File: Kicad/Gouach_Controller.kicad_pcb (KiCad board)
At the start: 4 copper layers, 41 x 104 mm, 139 parts, among them J1 HALL/Encoder, J10 USB, J11 CAN, J12 Serial, J2 Peripherals, J3 Peripherals, J4 IN+, J5 IN-, J6 MOTOR3, J7 MOTOR2, J8 MOTOR1, J9 SWD, Q1 IRFB7530, Q2 IRFB7530, Q3 IRFB7530, Q4 IRFB7530, Q5 IRFB7530, Q6 IRFB7530, Q7 DMN3300U, U1 STM32F405RGT6, U2 XC6220B331MR, U3 DRV8302, U4 SN65HVD232, U5 TPS54360DDA, U6 USBLC6-2SC6, Y2 8MHz

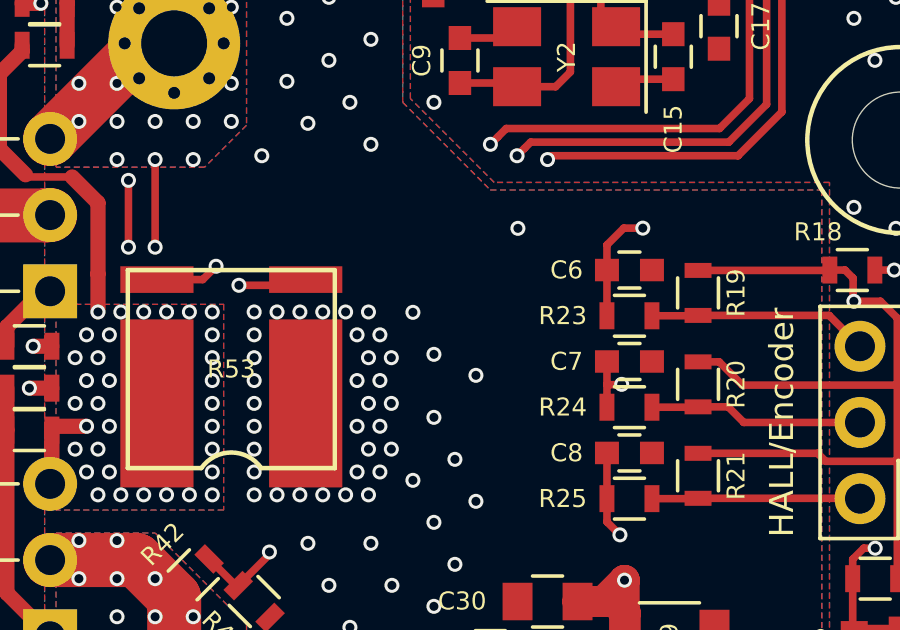
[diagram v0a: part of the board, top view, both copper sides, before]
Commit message: gouach logo
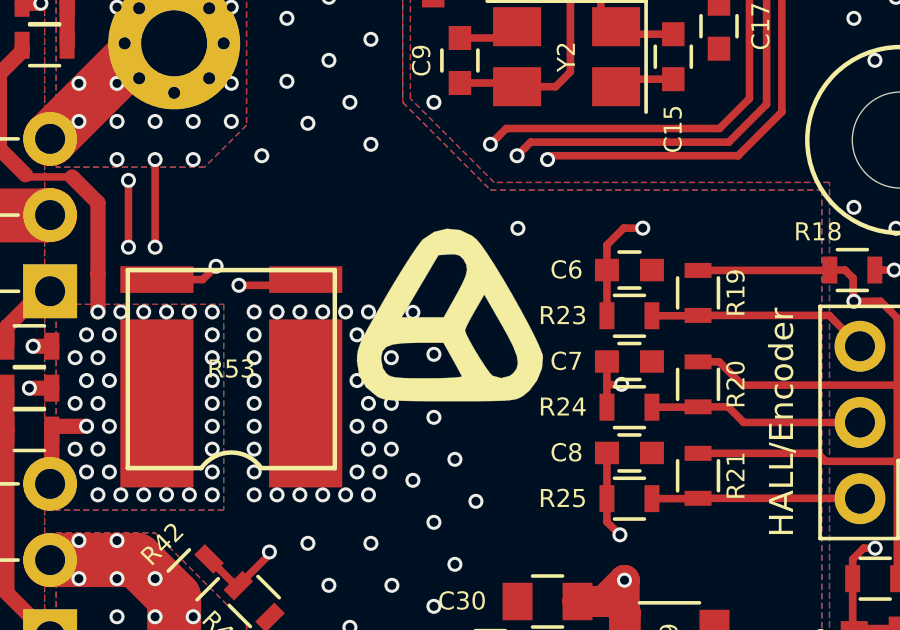
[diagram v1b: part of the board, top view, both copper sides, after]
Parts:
- removed the G*** at (120.4, 137.3)
- added G***: LOGO, logos:logotype, B.Cu at (119.5, 103.7)
- added G***: LOGO, logos:picto, F.Cu at (120.0, 85.6)
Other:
- board text added: "V1.0"

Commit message: changed all componenents to know version
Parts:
- removed G***: LOGO, logos:logotype
- removed G***: LOGO, logos:picto
- added U7: picto, logos:picto, F.Cu at (120.5, 87.1)
- added U8: logo, logos:logotype, B.Cu at (120.4, 97.4)
- C1, C10, C11, C12, C13, C14, C15, C16, C17, C18, C19, C2, C20, C21, C22, C23, C24, C25, C26, C27, C28, C32, C33, C34, C35, C36, C37, C39, C4, C46, C47, C5, C51, C52, C53, C56, C6, C7, C8, C9: footprint Capacitors_SMD:C_0603 -> Capacitor_SMD:C_0603_1608Metric
- C29, C3, C31, C49, C50, C55: footprint Capacitors_SMD:C_1210 -> Capacitor_SMD:C_1210_3225Metric
- C30, C38: footprint Capacitors_SMD:C_0805 -> Capacitor_SMD:C_0805_2012Metric
- C40, C41, C43, C44: footprint Capacitors_SMD:C_1206 -> Capacitor_SMD:C_1206_3216Metric
- C48: value 15uF/100V -> 15uF
- R1, R10, R11, R12, R13, R14, R15, R16, R17, R18, R19, R2, R20, R21, R22, R23, R24, R25, R26, R27, R28, R29, R3, R30, R31, R32, R33, R34, R35, R36, R37, R38, R39, R4, R40, R41, R42, R43, R44, R45, R46, R47, R5, R6, R7, R8, R9: footprint Resistors_SMD:R_0603 -> Resistor_SMD:R_0603_1608Metric
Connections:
- U1 pad 2: Net-(U1-Pad2) -> (no net)
- U1 pad 20: Net-(U1-Pad20) -> (no net)
- U1 pad 23: Net-(U1-Pad23) -> (no net)
- U1 pad 28: Net-(U1-Pad28) -> (no net)
- U1 pad 3: Net-(U1-Pad3) -> (no net)
- U1 pad 37: Net-(U1-Pad37) -> (no net)
- U1 pad 38: Net-(U1-Pad38) -> (no net)
- U1 pad 4: Net-(U1-Pad4) -> (no net)
- U1 pad 50: Net-(U1-Pad50) -> (no net)
- U1 pad 54: Net-(U1-Pad54) -> (no net)
- U1 pad 55: Net-(U1-Pad55) -> (no net)
- U1 pad 56: Net-(U1-Pad56) -> (no net)
- U2 pad 4: Net-(U2-Pad4) -> (no net)
- U3 pad 4: Net-(U3-Pad4) -> (no net)
- U3 pad 5: Net-(U3-Pad5) -> (no net)
- U3 pad 55: Net-(U3-Pad55) -> (no net)
- U3 pad 56: Net-(U3-Pad56) -> (no net)
- U4 pad 5: Net-(U4-Pad5) -> (no net)
- U4 pad 8: Net-(U4-Pad8) -> (no net)
- U5 pad 3: Net-(U5-Pad3) -> (no net)

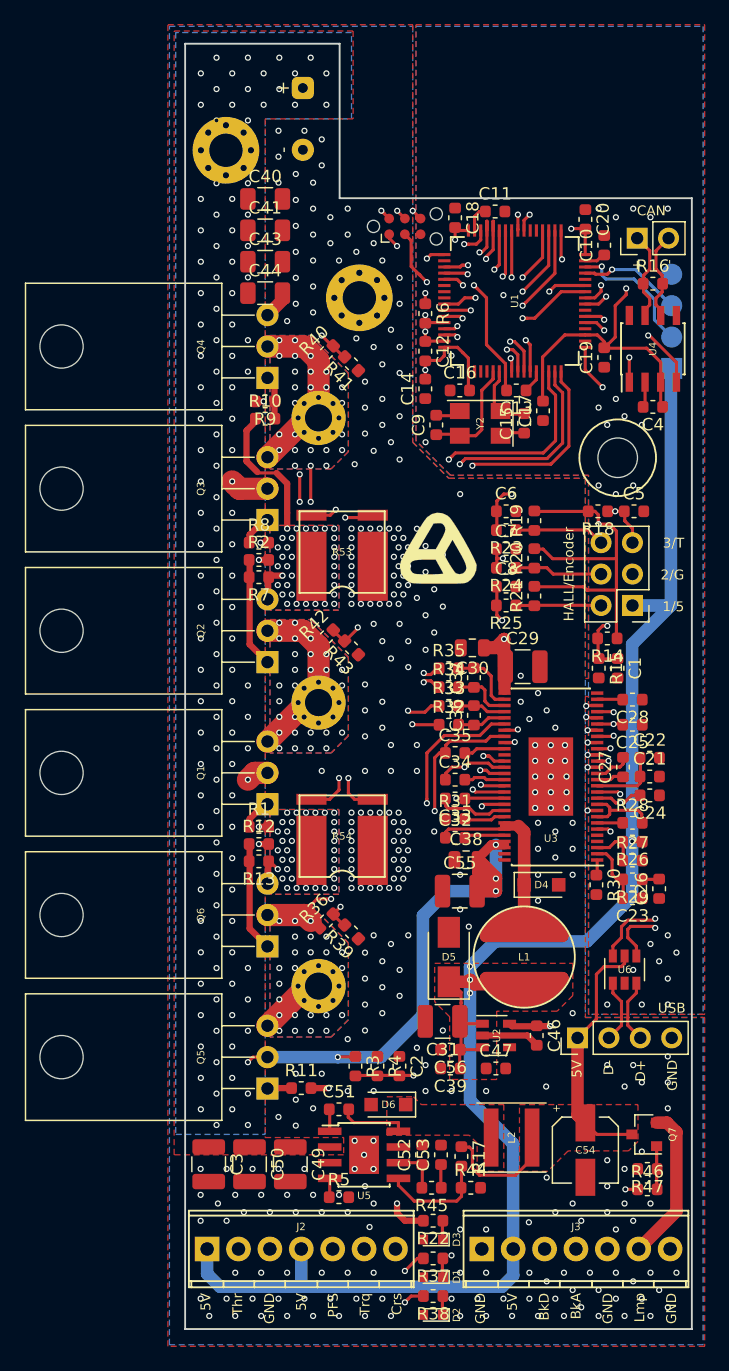
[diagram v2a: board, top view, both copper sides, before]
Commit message: Modified silkscreens. Changed peripheral connectors. Fixed some 3D libs paths
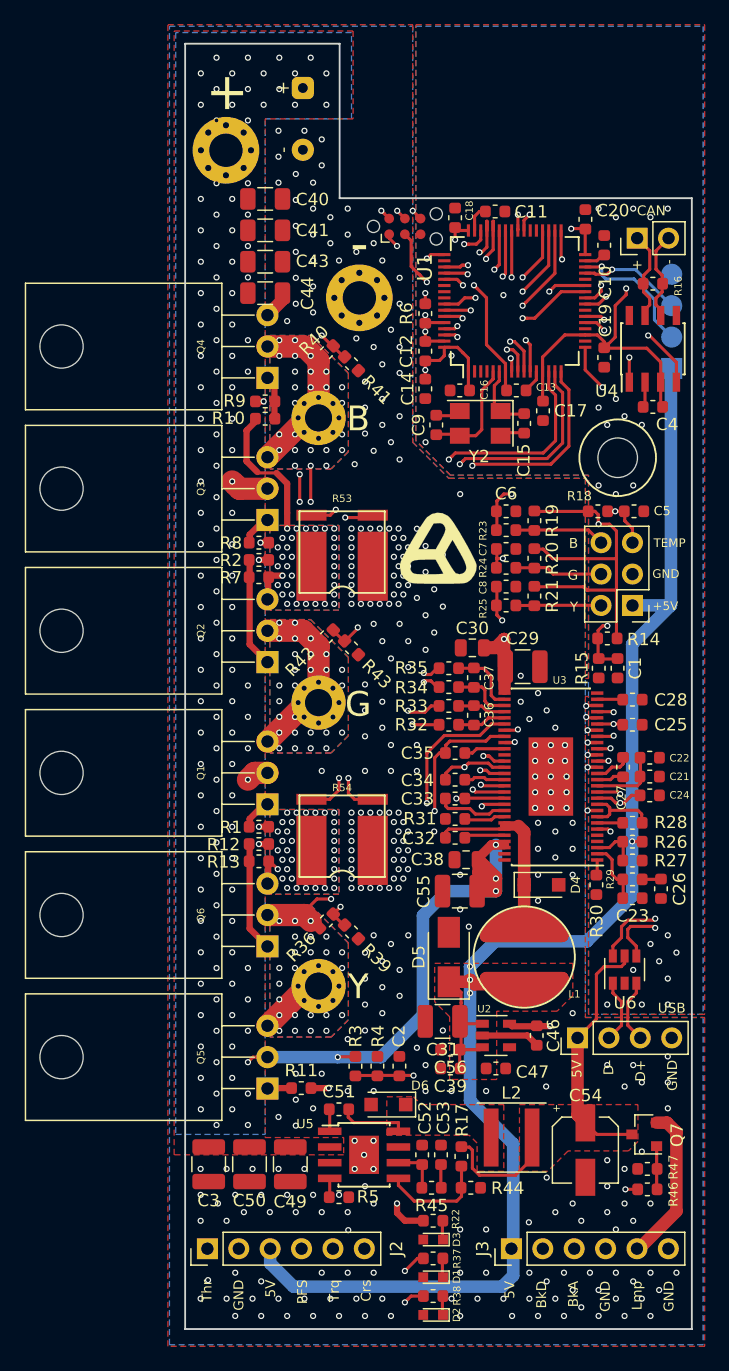
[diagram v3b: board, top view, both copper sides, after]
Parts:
- J2, J3: footprint Romain:TerminalBlock_Phoenix_MPT-2.54mm_7pol -> Connector_PinHeader_2.54mm:PinHeader_1x06_P2.54mm_Vertical
- moved J3 2.40 mm to (126.4, 143.5), turned to 90 degrees
- moved C26 0.15 mm to (138.5, 114.4)
- turned J2 to 90 degrees
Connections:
- J2 pad 1: +5V -> /ADC_THROTTLE
- J2 pad 2: /ADC_THROTTLE -> GND
- J2 pad 3: GND -> +5V
- J2 pad 4: +5V -> /PFS
- J2 pad 5: /PFS -> /ADC_TORQUE
- J2 pad 6: /ADC_TORQUE -> /CRUISE
- J3 pad 1: GND -> +5V
- J3 pad 2: +5V -> /IO_BRAKE
- J3 pad 3: /IO_BRAKE -> /ADC_BRAKE
- J3 pad 4: /ADC_BRAKE -> GND
- J3 pad 5: GND -> Net-(J3-Pad5)
- J3 pad 6: Net-(J3-Pad6) -> GND
- Q7 pad 2: Net-(J3-Pad6) -> Net-(J3-Pad5)
- U1 pad 2: (no net) -> Net-(U1-Pad2)
- U1 pad 20: (no net) -> Net-(U1-Pad20)
- U1 pad 23: (no net) -> Net-(U1-Pad23)
- U1 pad 28: (no net) -> Net-(U1-Pad28)
- U1 pad 3: (no net) -> Net-(U1-Pad3)
- U1 pad 37: (no net) -> Net-(U1-Pad37)
- U1 pad 38: (no net) -> Net-(U1-Pad38)
- U1 pad 4: (no net) -> Net-(U1-Pad4)
- U1 pad 50: (no net) -> Net-(U1-Pad50)
- U1 pad 54: (no net) -> Net-(U1-Pad54)
- U1 pad 55: (no net) -> Net-(U1-Pad55)
- U1 pad 56: (no net) -> Net-(U1-Pad56)
- U2 pad 4: (no net) -> Net-(U2-Pad4)
- U3 pad 4: (no net) -> Net-(U3-Pad4)
- U3 pad 5: (no net) -> Net-(U3-Pad5)
- U3 pad 55: (no net) -> Net-(U3-Pad55)
- U3 pad 56: (no net) -> Net-(U3-Pad56)
- U4 pad 5: (no net) -> Net-(U4-Pad5)
- U4 pad 8: (no net) -> Net-(U4-Pad8)
- U5 pad 3: (no net) -> Net-(U5-Pad3)
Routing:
- net Net-(J3-Pad6): track 12.6 -> 0.00 mm
- net Net-(J3-Pad5): track 0.00 -> 12.6 mm
- net +5V: track 138.0 -> 129.3 mm
- net /ADC_TORQUE: track 90.9 -> 94.5 mm
- net /ADC_THROTTLE: track 99.6 -> 103.0 mm
- net /PFS: track 95.5 -> 98.0 mm
- net /CRUISE: track 107.6 -> 109.3 mm
- net GND: vias 328 -> 324
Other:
- board text added: "+"
- board text added: "+5V"
- board text added: "-"
- board text added: "5V BkD BkA GND Lmp GND"
- board text added: "B"
- board text added: "B G Y"
- board text added: "G"
- board text added: "GND"
- board text added: "TEMP"
- board text added: "TEMP B GND G +5V Y"
- board text added: "Thr GND 5V PFS Trq Crs"
- board text added: "Y"
- board text removed: "3/T 2/G 1/5"
- board text removed: "5V Thr GND 5V PFS Trq Crs"
- board text removed: "GND 5V BkD BkA GND Lmp GND"
- board text removed: "TEMP HALL3 GND HALL2 +5V HALL1"
